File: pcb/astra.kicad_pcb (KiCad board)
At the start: 4 copper layers, 42.6 x 43.4 mm, 91 parts, among them J1 Conn_01x02_Pin, J2 Conn_02x11_Odd_Even, J3 Conn_01x04_MountingPin, M1 Motor_DC, M2 Motor_DC, M3 Motor_DC, M4 Motor_DC, Q1 AO3400A, Q2 AO3400A, Q3 AO3400A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

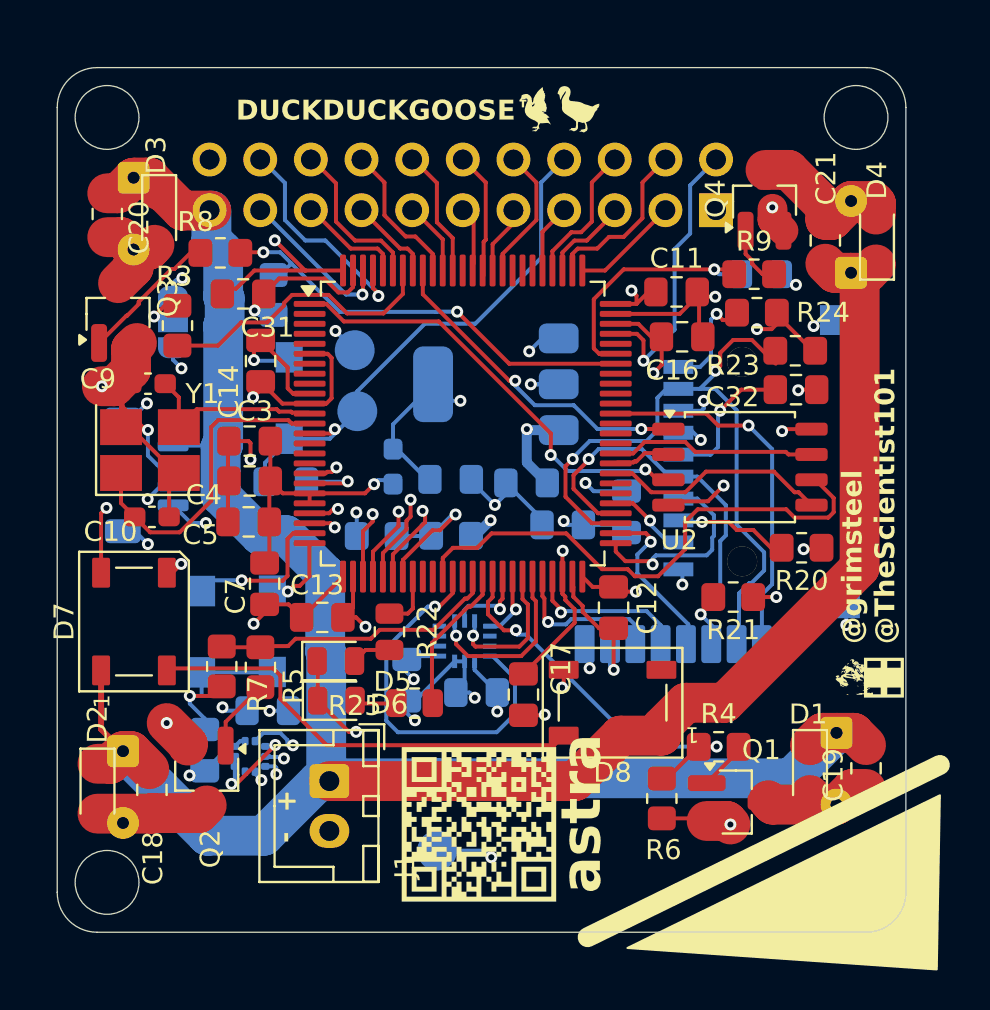
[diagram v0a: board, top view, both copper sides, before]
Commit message: [pcb] dogbone board edge for mounting holes
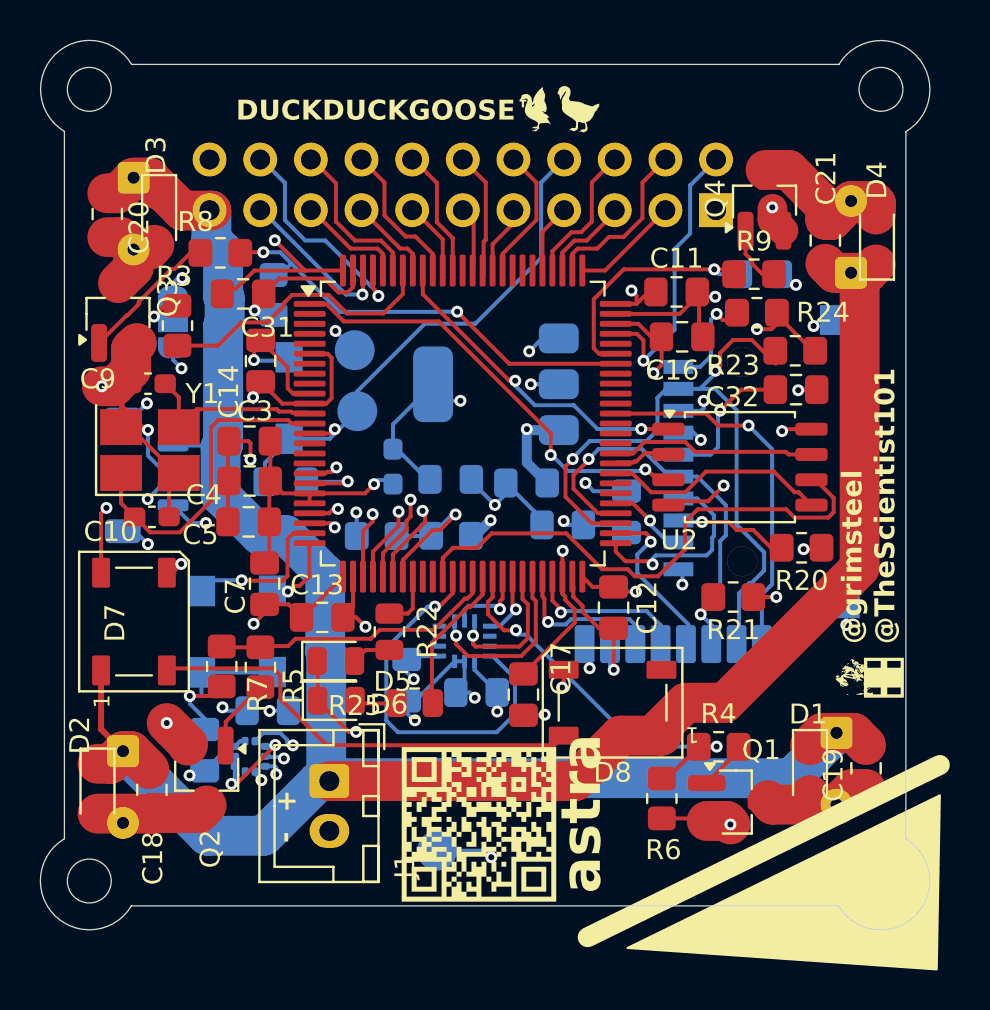
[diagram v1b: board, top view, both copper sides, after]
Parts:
- removed the REF** at (126.8, 39.4)
- removed the REF** at (164.4, 77.7)
- removed the REF** at (126.8, 77.7)
- removed the REF** at (164.4, 39.4)
- added REF**: MountingHole_2.2mm_M2, MountingHole:MountingHole_2.2mm_M2, F.Cu at (165.6, 38.0)
- added REF**: MountingHole_2.2mm_M2, MountingHole:MountingHole_2.2mm_M2, F.Cu at (125.9, 77.7)
- added REF**: MountingHole_2.2mm_M2, MountingHole:MountingHole_2.2mm_M2, F.Cu at (125.9, 38.0)
- added REF**: MountingHole_2.2mm_M2, MountingHole:MountingHole_2.2mm_M2, F.Cu at (165.6, 77.7)
- moved G*** 1.41 mm to (132.9, 75.2)
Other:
- board size 42.6 x 43.4 mm -> 44.6 x 44.6 mm

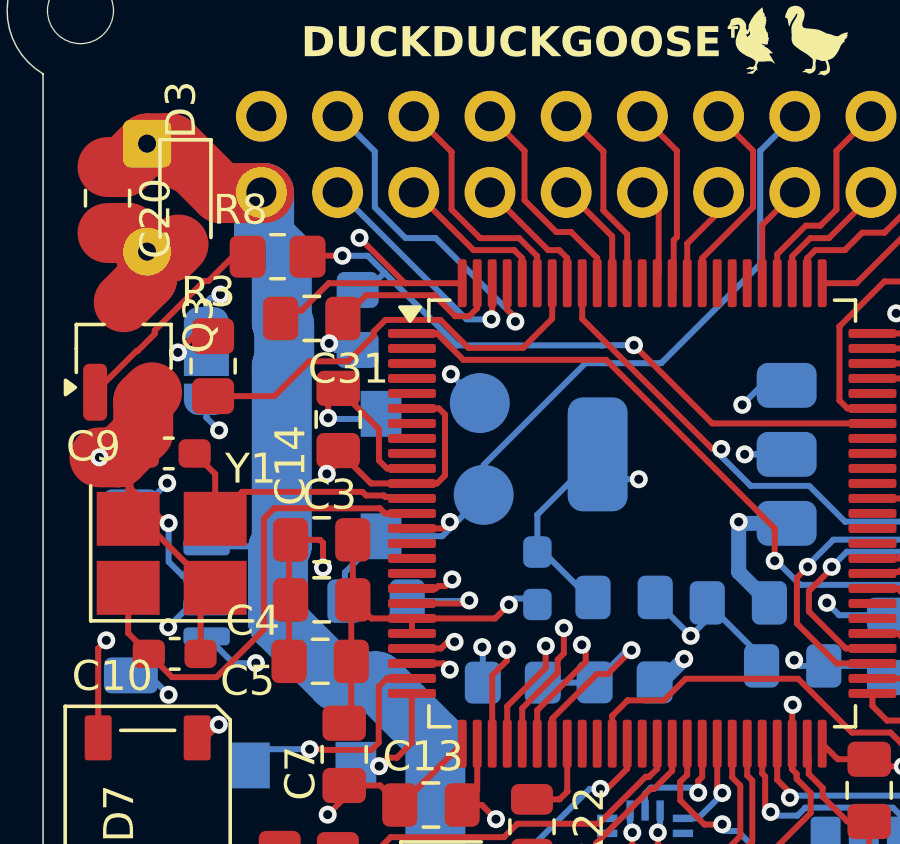
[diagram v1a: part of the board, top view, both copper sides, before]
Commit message: [pcb] various routing improvements
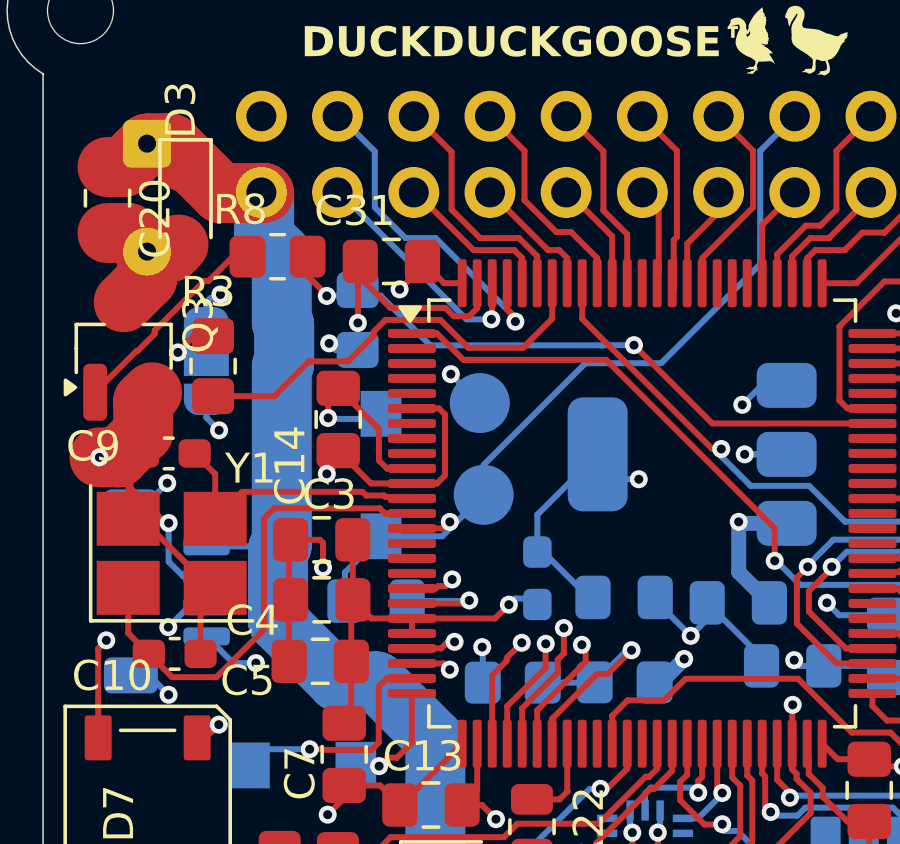
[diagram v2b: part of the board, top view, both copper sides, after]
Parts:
- moved C31 3.26 mm to (136.3, 46.3), turned to 180 degrees
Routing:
- net +3.3V: track 66.3 -> 151.8 mm
- net GND: track 124.3 -> 125.3 mm, vias 37 -> 38
- net BAR_CS: track 21.9 -> 22.8 mm

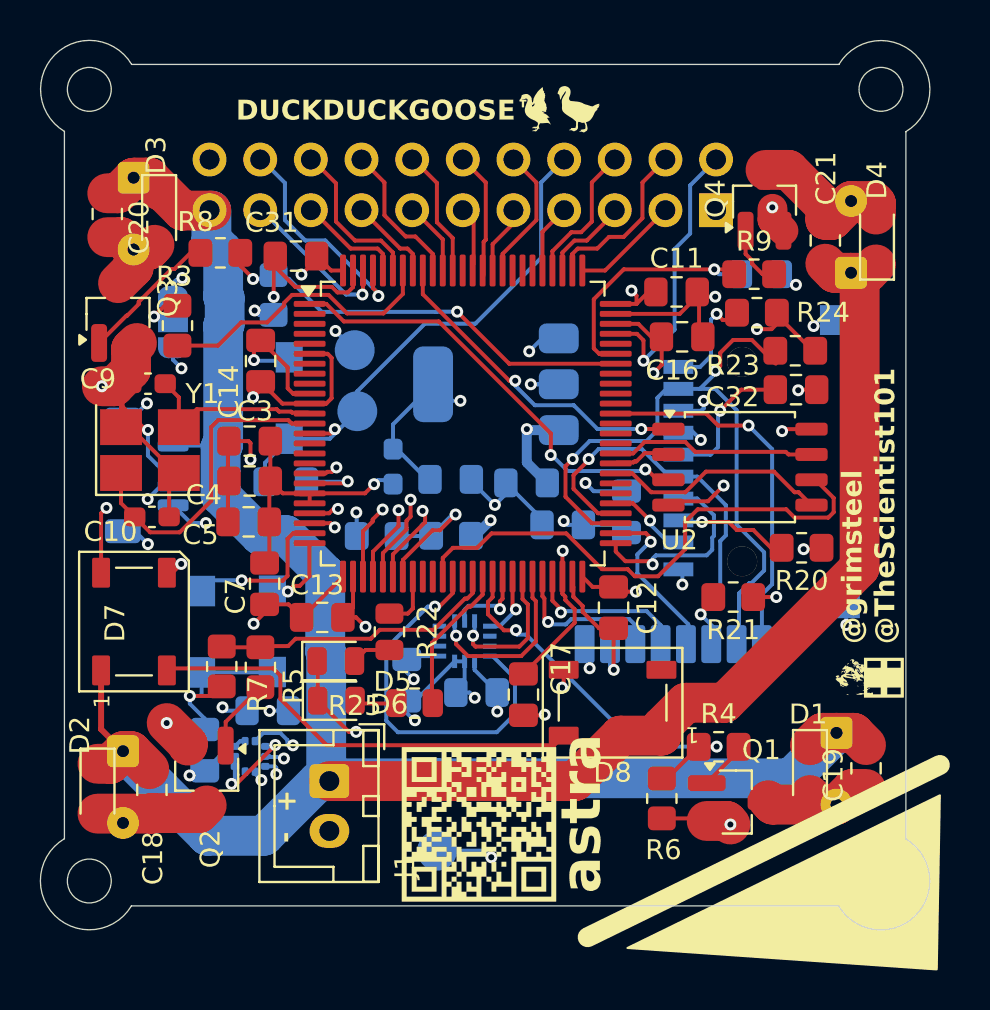
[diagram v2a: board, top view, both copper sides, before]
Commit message: [pcb] reroute front traces under stm32
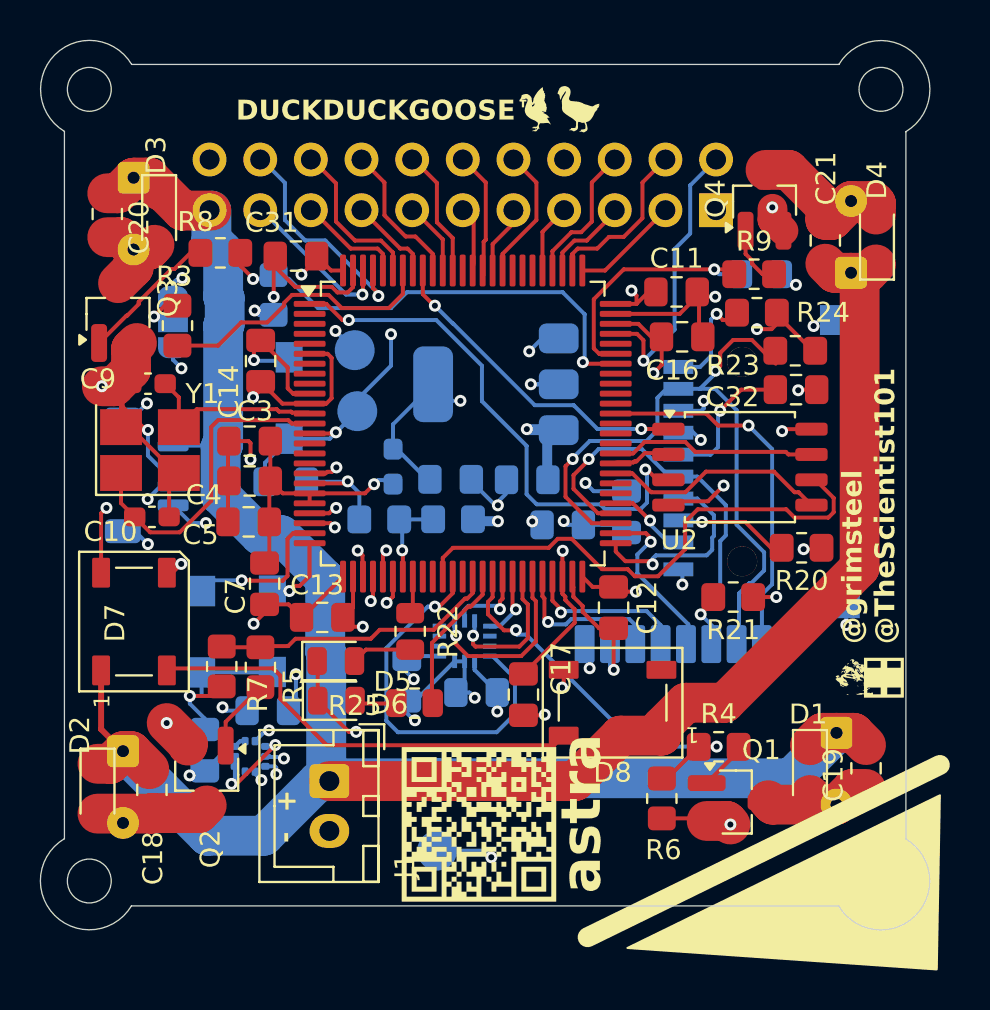
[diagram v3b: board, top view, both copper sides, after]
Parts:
- moved R22 1.04 mm to (142.0, 65.1)
- moved R2 0.84 mm to (140.4, 59.5)
- moved R1 0.84 mm to (144.2, 59.5)
- moved C1 0.16 mm to (147.9, 57.5)
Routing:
- net SPI1_CLK: track 20.3 -> 10.8 mm
- net SPI1_MOSI: track 21.0 -> 12.4 mm
- net SPI1_MISO: track 24.4 -> 16.6 mm
- net BAR_CS: track 22.8 -> 15.9 mm
- net FLASH_IO_2: track 21.8 -> 26.3 mm
- net BAT_MEASURE: track 7.81 -> 4.65 mm
- net MOTOR3: track 21.6 -> 23.7 mm
- net +3.3V: track 151.8 -> 149.9 mm
- net Net-(D5-A): track 1.98 -> 3.03 mm
- net STATUS_LED_1: track 2.89 -> 1.89 mm
- net GND: track 125.3 -> 124.3 mm
- net +BATT: track 172.7 -> 173.4 mm
- net RST: track 26.6 -> 26.0 mm, vias 1 -> 2
